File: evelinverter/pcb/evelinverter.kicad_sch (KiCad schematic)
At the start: 11 parts, among them J1 IN+, J10 enc, J11 hall, J2 IN-, J3 swd, J4 U, J5 V, J6 W, J7 spi, J8 uart, J9 i2c

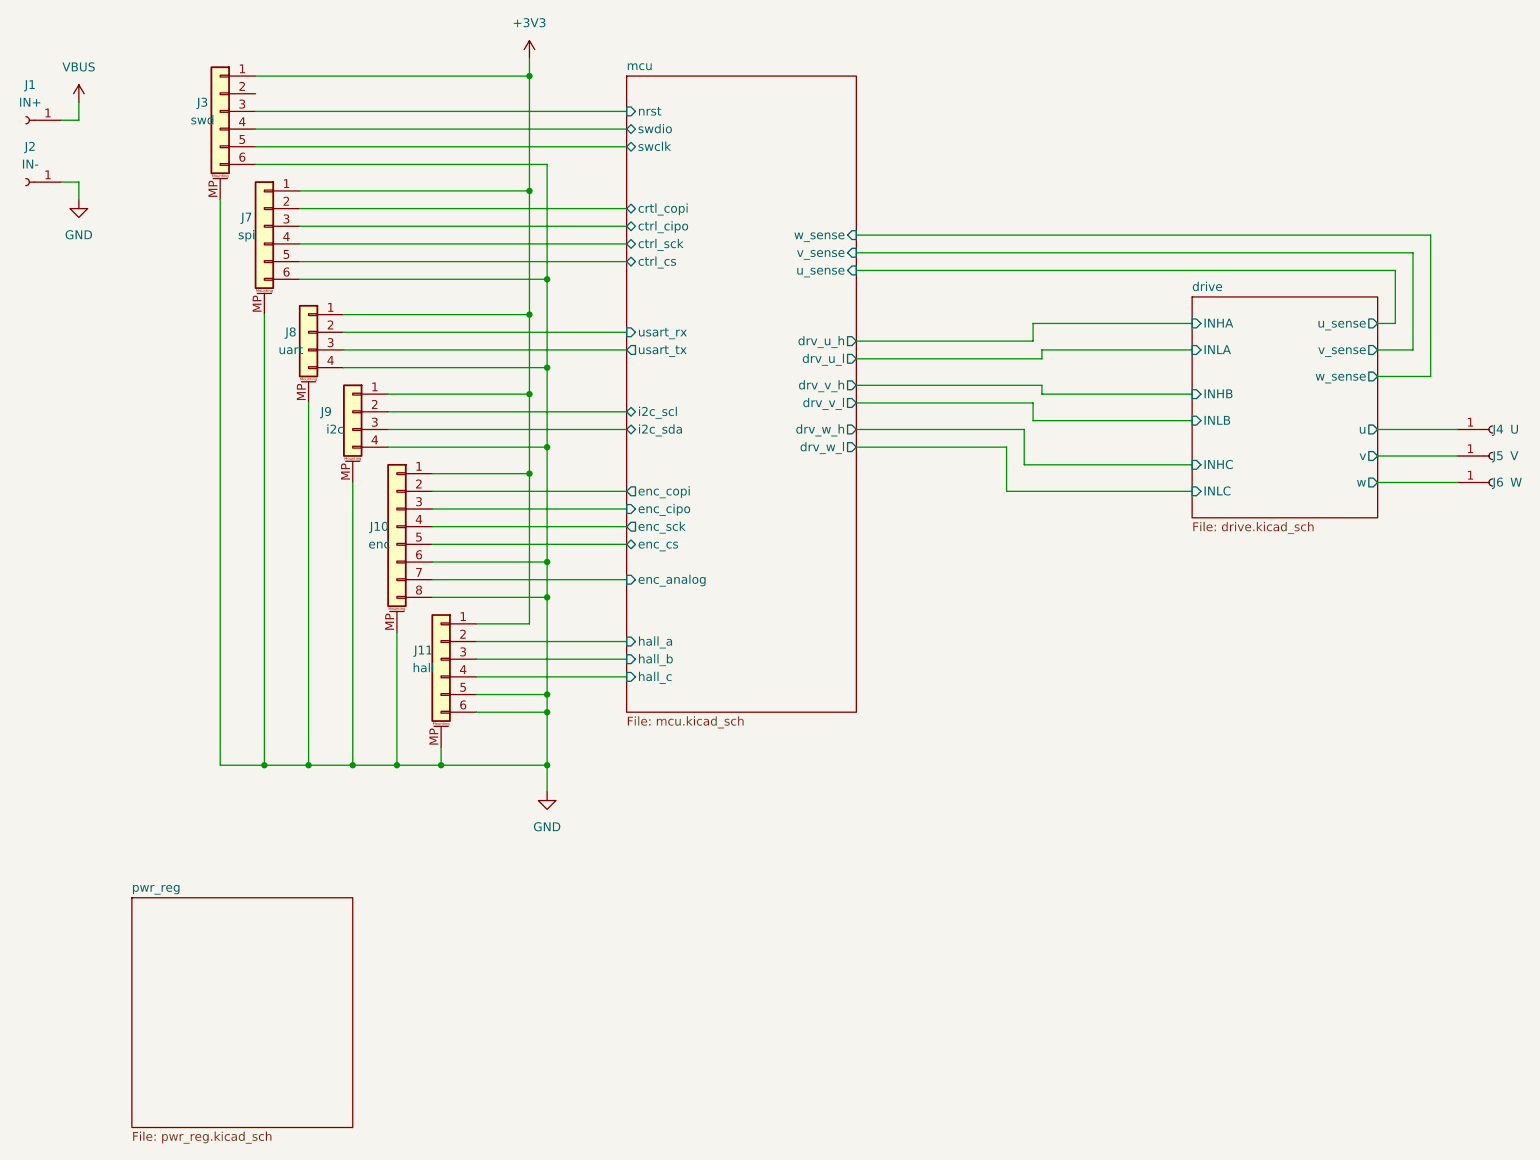
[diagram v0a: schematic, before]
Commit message: started redoing evelinverter
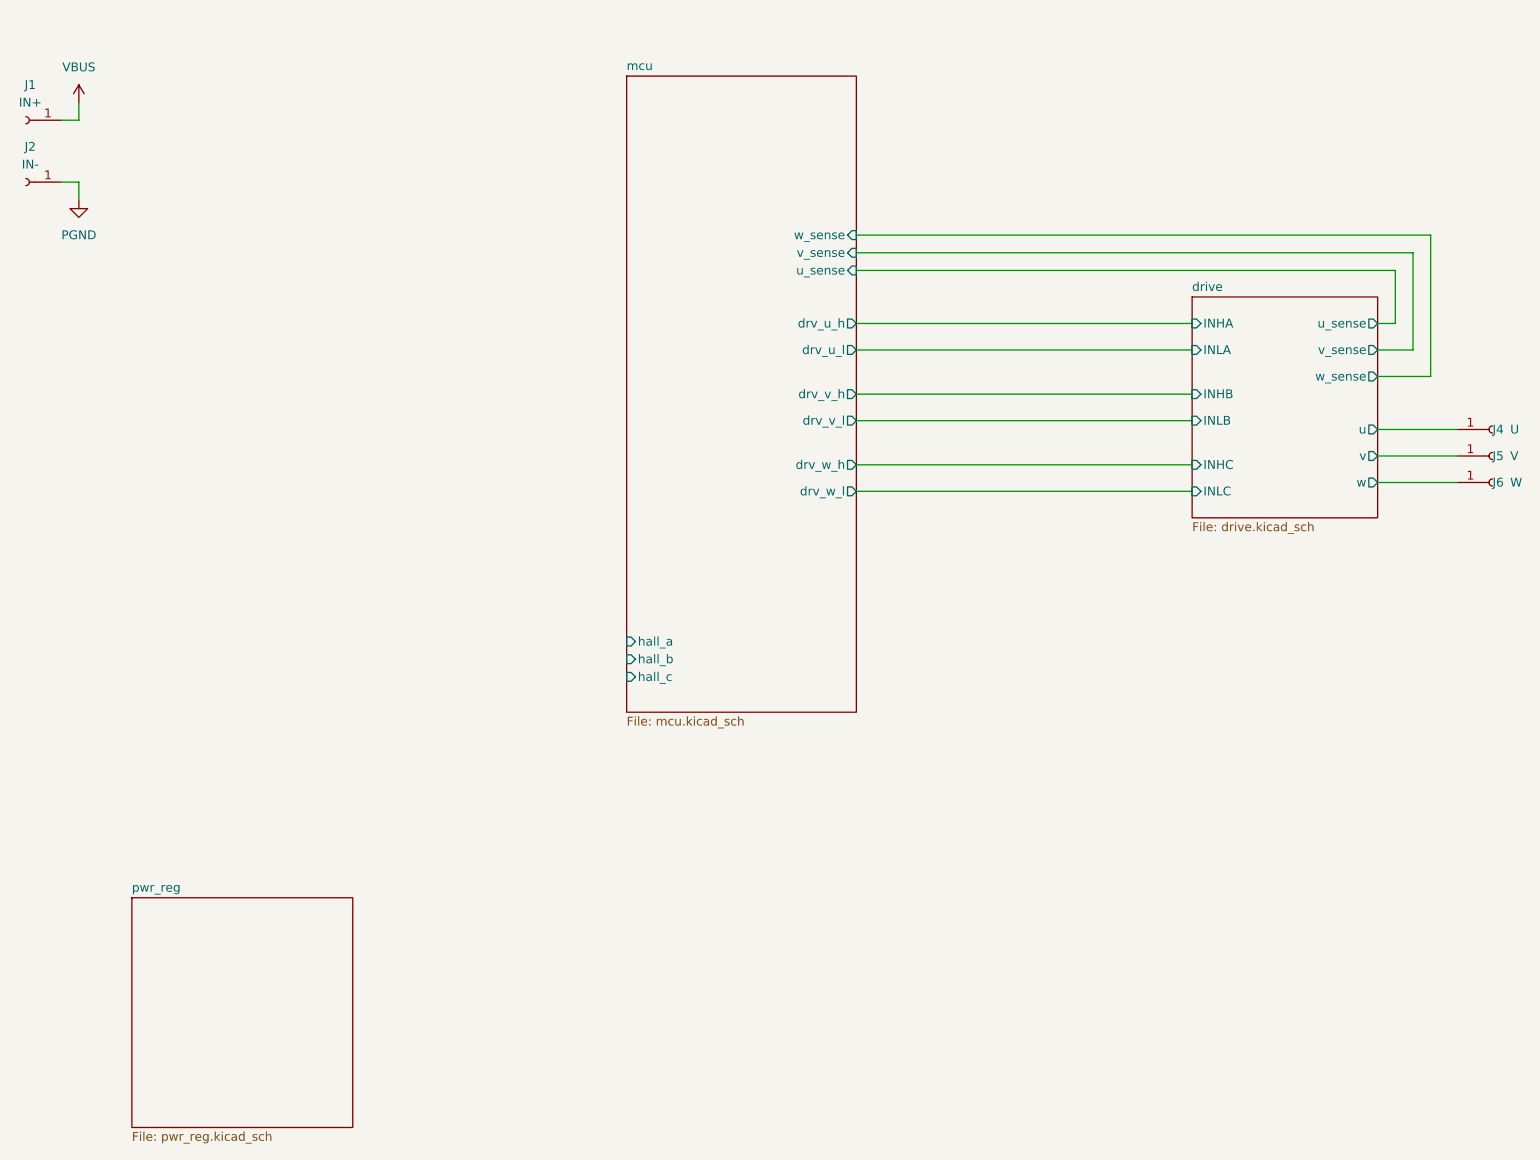
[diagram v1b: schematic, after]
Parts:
- removed J10: enc, a22verter:MOLEX_5055670851, symbol Connector_Generic_MountingPin:Conn_01x08_MountingPin
- removed J11: hall, a22verter:MOLEX_5055670651, symbol Connector_Generic_MountingPin:Conn_01x06_MountingPin
- removed J3: swd, a22verter:MOLEX_5055670651, symbol Connector_Generic_MountingPin:Conn_01x06_MountingPin
- removed J7: spi, a22verter:MOLEX_5055670651, symbol Connector_Generic_MountingPin:Conn_01x06_MountingPin
- removed J8: uart, a22verter:MOLEX_5055670451, symbol Connector_Generic_MountingPin:Conn_01x04_MountingPin
- removed J9: i2c, a22verter:MOLEX_5055670451, symbol Connector_Generic_MountingPin:Conn_01x04_MountingPin
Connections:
- net GND renamed PGND
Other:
- sheet mcu ports: added none; removed crtl_copi, ctrl_cipo, ctrl_cs, ctrl_sck, enc_analog, enc_cipo, enc_copi, enc_cs, enc_sck, i2c_scl, i2c_sda, nrst, swclk, swdio, usart_rx, usart_tx
